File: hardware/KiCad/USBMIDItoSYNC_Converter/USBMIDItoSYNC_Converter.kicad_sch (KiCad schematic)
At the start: 19 parts, among them J1 MJ8435, J2 MJ8435, J3 MJ8435, SW1 SW_SPDT, SW2 SW_DIP_x04, U1 MOUDLE-SEEEDUINO-XIAO, U2 TLP2368_TPL,E, U3 SN74LV1T34DBVR

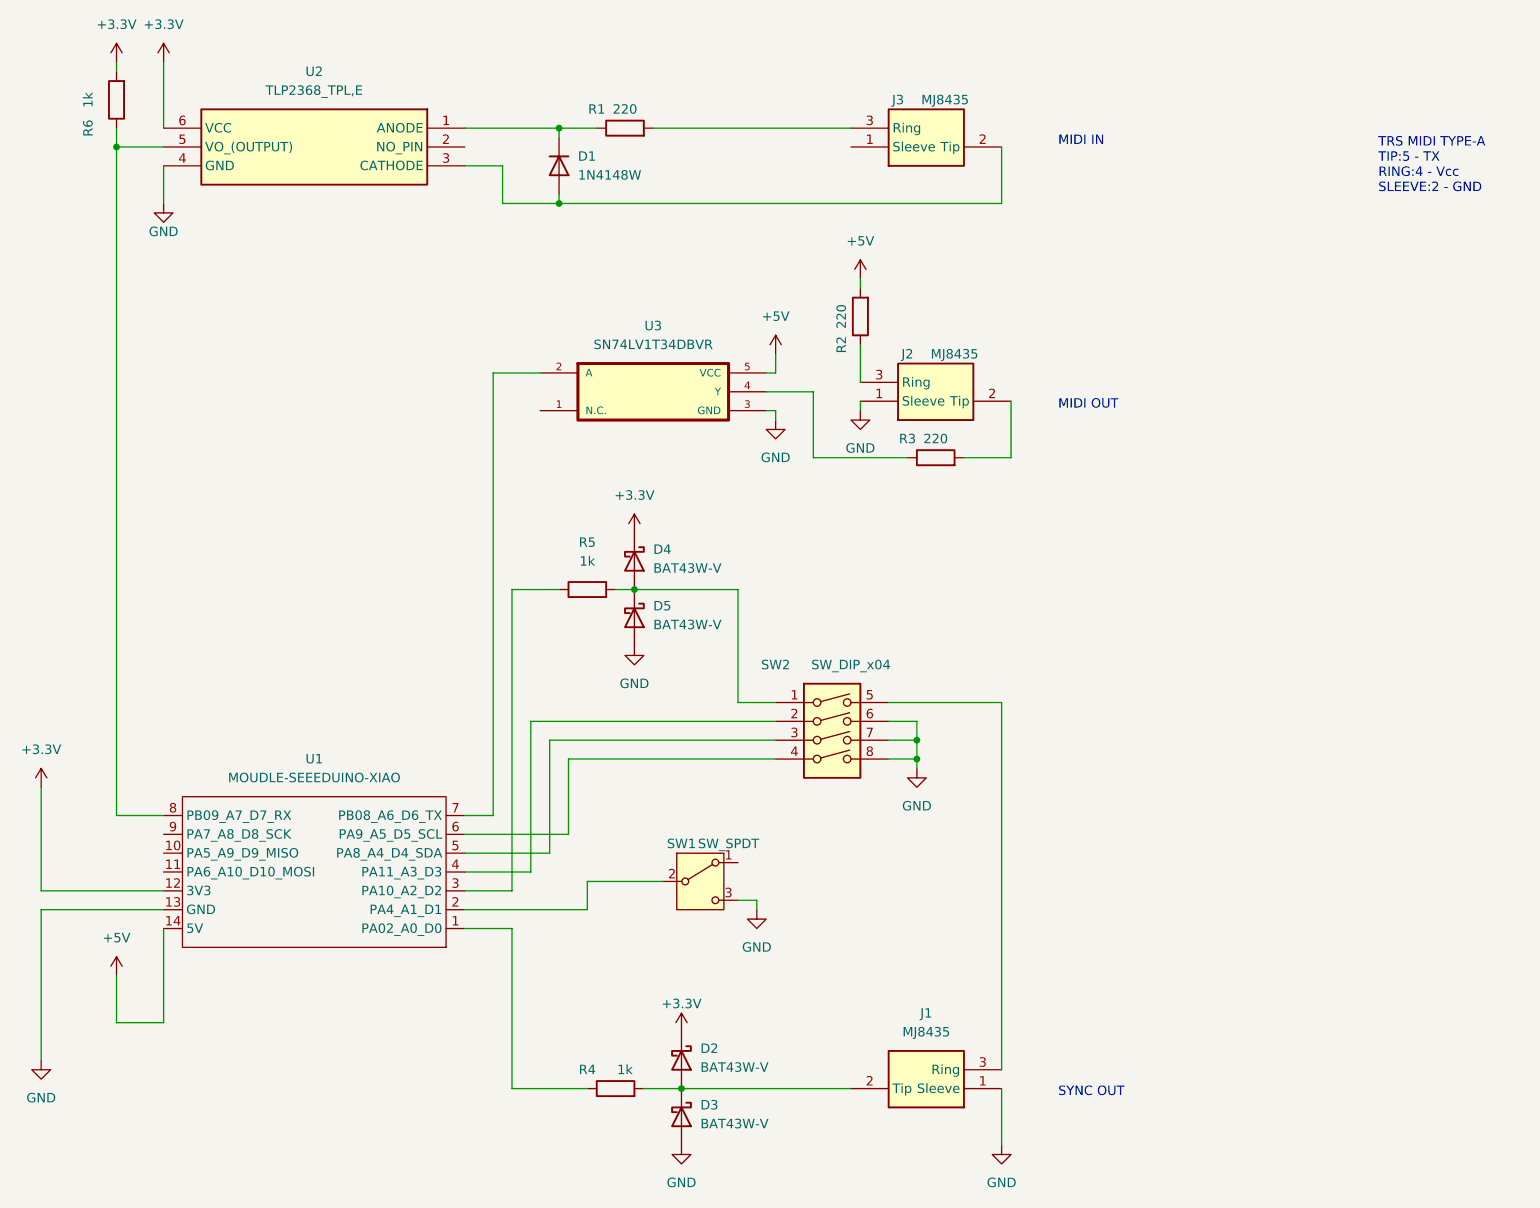
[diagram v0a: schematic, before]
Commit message: fix schematic :  protection circuit
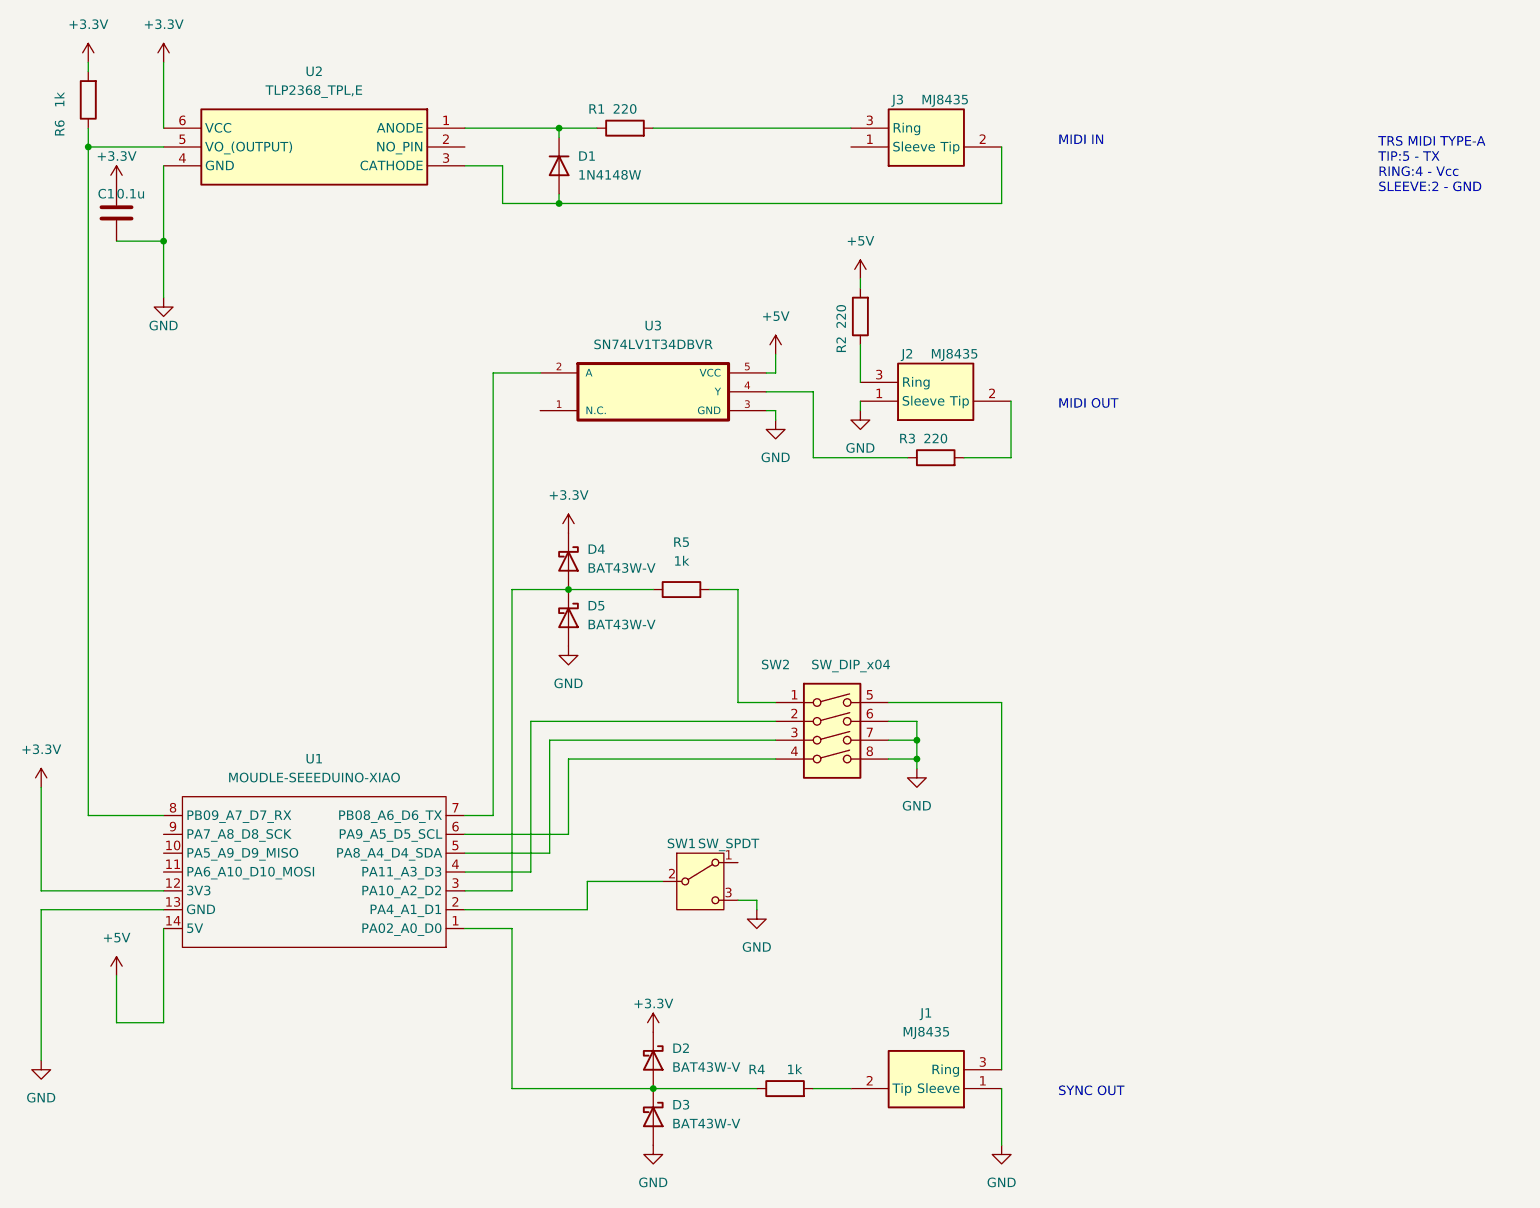
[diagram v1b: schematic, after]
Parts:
- added C1: 0.1u, Capacitor_SMD:C_0603_1608Metric, symbol Device:C
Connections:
- net +3.3V: now also C1.1
- net GND: now also C1.2
- net at D4.2 (A), D5.1 (K): now also R5.1, U1.3 (PA10_A2_D2); no longer R5.2, SW2.1
- net at R4.1, U1.1 (PA02_A0_D0): now also D2.2 (A), D3.1 (K)
- net at J1.2 (Tip), R4.2: no longer D2.2 (A), D3.1 (K)
- new net: R5.2, SW2.1
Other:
- moved on the sheet: D2, D3, D4, D5, R4, R5, R6
